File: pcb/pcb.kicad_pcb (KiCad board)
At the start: 2 copper layers, 63 parts, among them J1 AMT0440007DB0000G, J10 Conn_02x10_Odd_Even, J11 Conn_01x03, J12 Conn_01x02, J15 Conn_01x10, J16 Conn_01x10, J2 AMT0440007DB0000G, J3 AMT0440007DB0000G, J4 AMT0440007DB0000G, J5 Conn_01x03, J6 Conn_01x03, J7 Conn_01x03, J8 Conn_01x03, J9 Conn_01x03, Q1 IRF9Z34NPBF, Q2 IRF9Z34NPBF, Q3 IRF9Z34NPBF, Q4 IRF9Z34NPBF, Q5 IRF9Z34NPBF, U1 ACS711ELCTR-12AB-T, U2 ACS711ELCTR-12AB-T, U3 ACS711ELCTR-12AB-T, U4 ACS711ELCTR-12AB-T, U5 ACS711ELCTR-12AB-T, U6 TXS0102DCUR, U7 TXS0102DCUR, U8 TXS0102DCUR, U9 NCP718BSNADJT1G

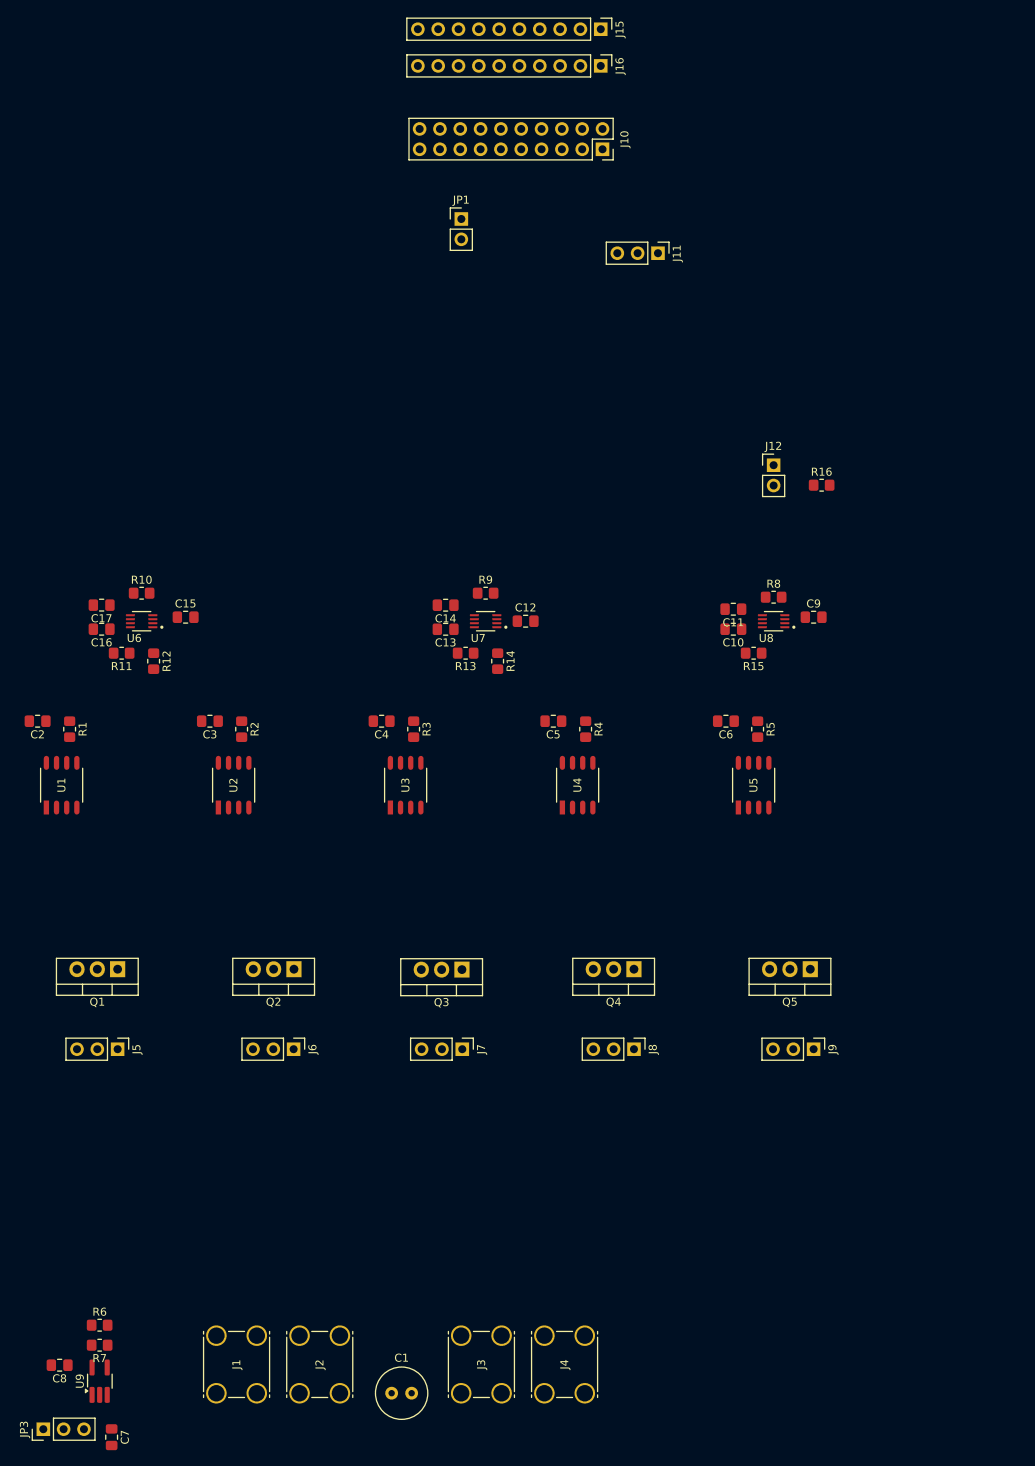
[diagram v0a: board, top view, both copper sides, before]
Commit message: Add missing power supply ctrl header and move STM32 header labels
The header for connecting the power supply control wires to the PCB was
missing from the schematic. This commit adds that header and makes the
schematic more clear with respect to the JST connector signals, the
signals associated with the wires from the JST connector, and the
signals that are routed to the STM32.

This commit also rearranges the STM32 header labels to be easier to
route.
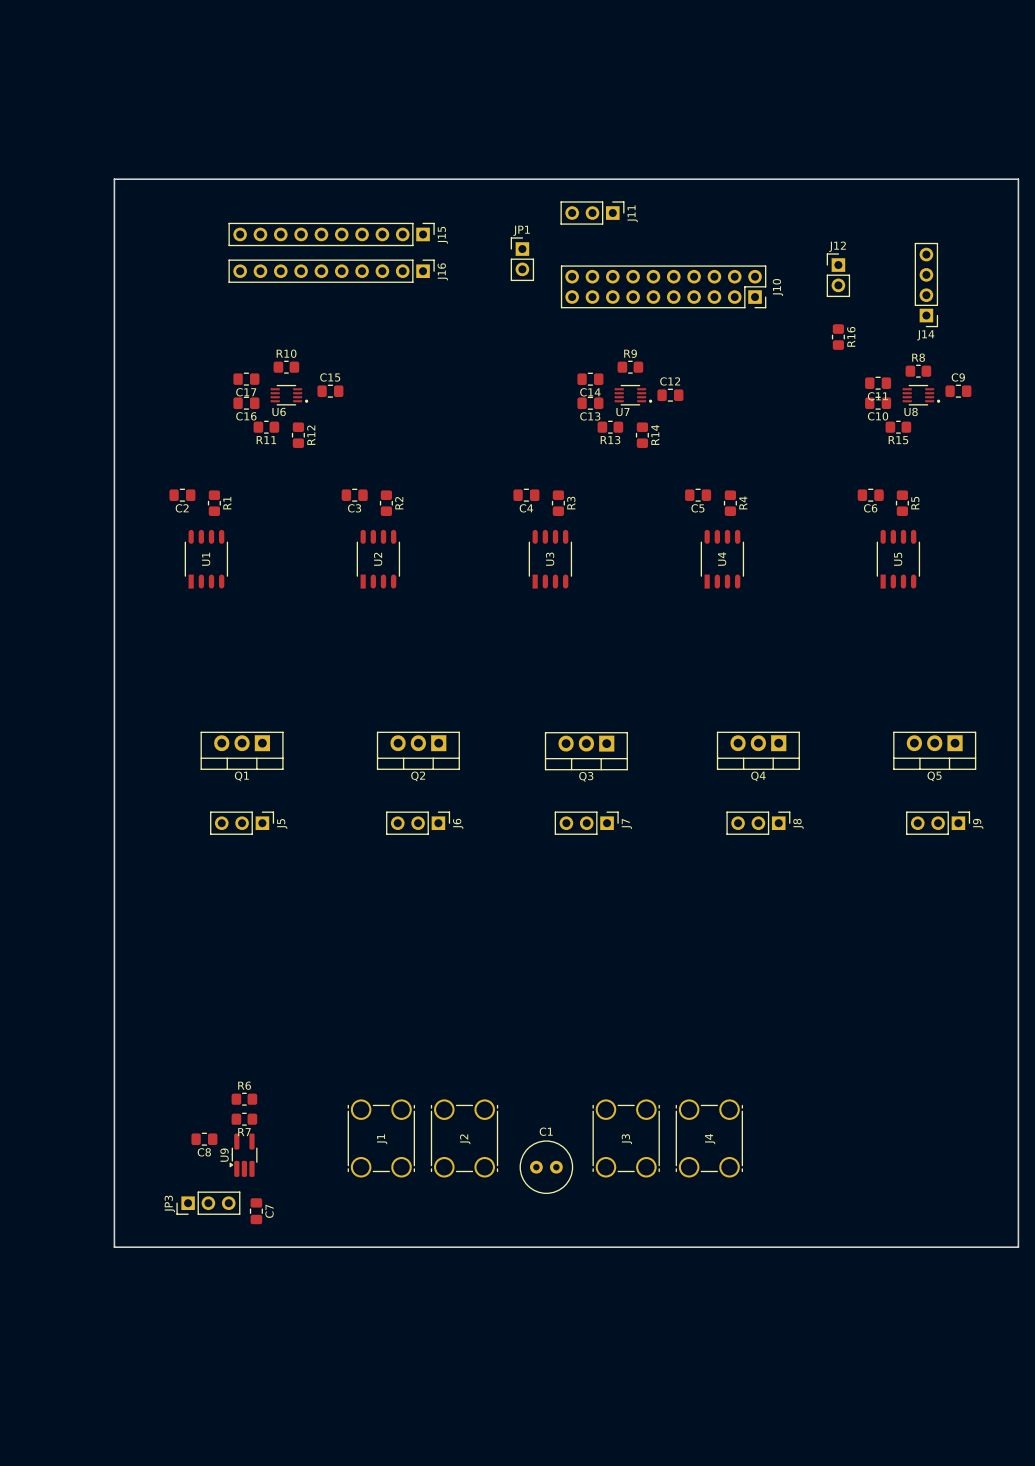
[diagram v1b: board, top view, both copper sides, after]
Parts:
- added J14: Conn_01x04, Connector_PinHeader_2.54mm:PinHeader_1x04_P2.54mm_Vertical, F.Cu at (193.1, 42.8)
- moved J16 33.9 mm to (130.2, 37.2)
- moved J15 33.9 mm to (130.2, 32.7)
- moved C13 33.5 mm to (151.1, 53.8)
- moved J2 33.5 mm to (132.8, 149.3)
- moved JP3 33.5 mm to (100.8, 153.8)
- moved C1 33.5 mm to (144.3, 149.2)
- moved C10 33.5 mm to (187.1, 53.8)
- moved C11 33.5 mm to (187.1, 51.2)
- moved C12 33.5 mm to (161.1, 52.8)
- moved C14 33.5 mm to (151.1, 50.8)
- moved C15 33.5 mm to (118.6, 52.2)
- moved C16 33.5 mm to (108.1, 53.8)
- moved C2 33.5 mm to (100.1, 65.2)
- moved C3 33.5 mm to (121.6, 65.2)
- moved C4 33.5 mm to (143.1, 65.2)
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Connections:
- J10 pad 1: CTRL_HIP -> I_SENSE_ELBOW
- J10 pad 10: I_SENSE_HAND -> SHUTOFF_WRIST_L
- J10 pad 11: SHUTOFF_HIP_L -> CTRL_HAND
- J10 pad 12: Net-(J10-Pin_12) -> I_SENSE_WRIST
- J10 pad 13: SHUTOFF_SHOULDER_L -> I_SENSE_HIP
- J10 pad 14: UART_STM_RX -> Net-(J10-Pin_14)
- J10 pad 15: SHUTOFF_ELBOW_L -> SHUTOFF_HIP_L
- J10 pad 16: UART_STM_TX -> UART_STM_RX
- J10 pad 17: SHUTOFF_WRIST_L -> CTRL_HIP
- J10 pad 18: +3V3 -> UART_STM_TX
- J10 pad 19: SHUTOFF_HAND_L -> +3V3
- J10 pad 2: I_SENSE_HIP -> CTRL_SHOULDER
- J10 pad 3: CTRL_HAND -> SHUTOFF_ELBOW_L
- J10 pad 4: I_SENSE_SHOULDER -> SHUTOFF_SHOULDER_L
- J10 pad 6: I_SENSE_ELBOW -> I_SENSE_SHOULDER
- J10 pad 7: CTRL_WRIST -> I_SENSE_HAND
- J10 pad 8: I_SENSE_WRIST -> CTRL_WRIST
- J10 pad 9: CTRL_SHOULDER -> SHUTOFF_HAND_L
- JP1 pad 1: Net-(J10-Pin_12) -> Net-(J10-Pin_14)
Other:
- board outline added: 113 x 133.5 mm

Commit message: Move +5V regulator to low power side of PCB
The +5V regulator was a bit cramped on the high-power side of the board
with the +7V and ground planes. Moving it to the low side gives those
planes more room and brings the +5V source closer to where it's used.
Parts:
- moved C7 102.1 mm to (96.5, 53.5), turned to 180 degrees
- moved C8 96.2 mm to (96.5, 49.8)
- moved R6 96.2 mm to (101.5, 44.8)
- moved R7 96.2 mm to (101.5, 47.3)
- moved U9 96.2 mm to (101.5, 51.8)
- moved JP3 95.3 mm to (102.5, 58.5), turned to -90 degrees
- moved R16 14.4 mm to (196.5, 45.5)
- moved C1 7.75 mm to (144.3, 141.5)
- moved J1 7.75 mm to (122.4, 141.5)
- moved J2 7.75 mm to (132.8, 141.5)
- moved J3 7.75 mm to (153.0, 141.5)
- moved J4 7.75 mm to (163.4, 141.5)
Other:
- board size 113 x 133.5 mm -> 110 x 123.8 mm

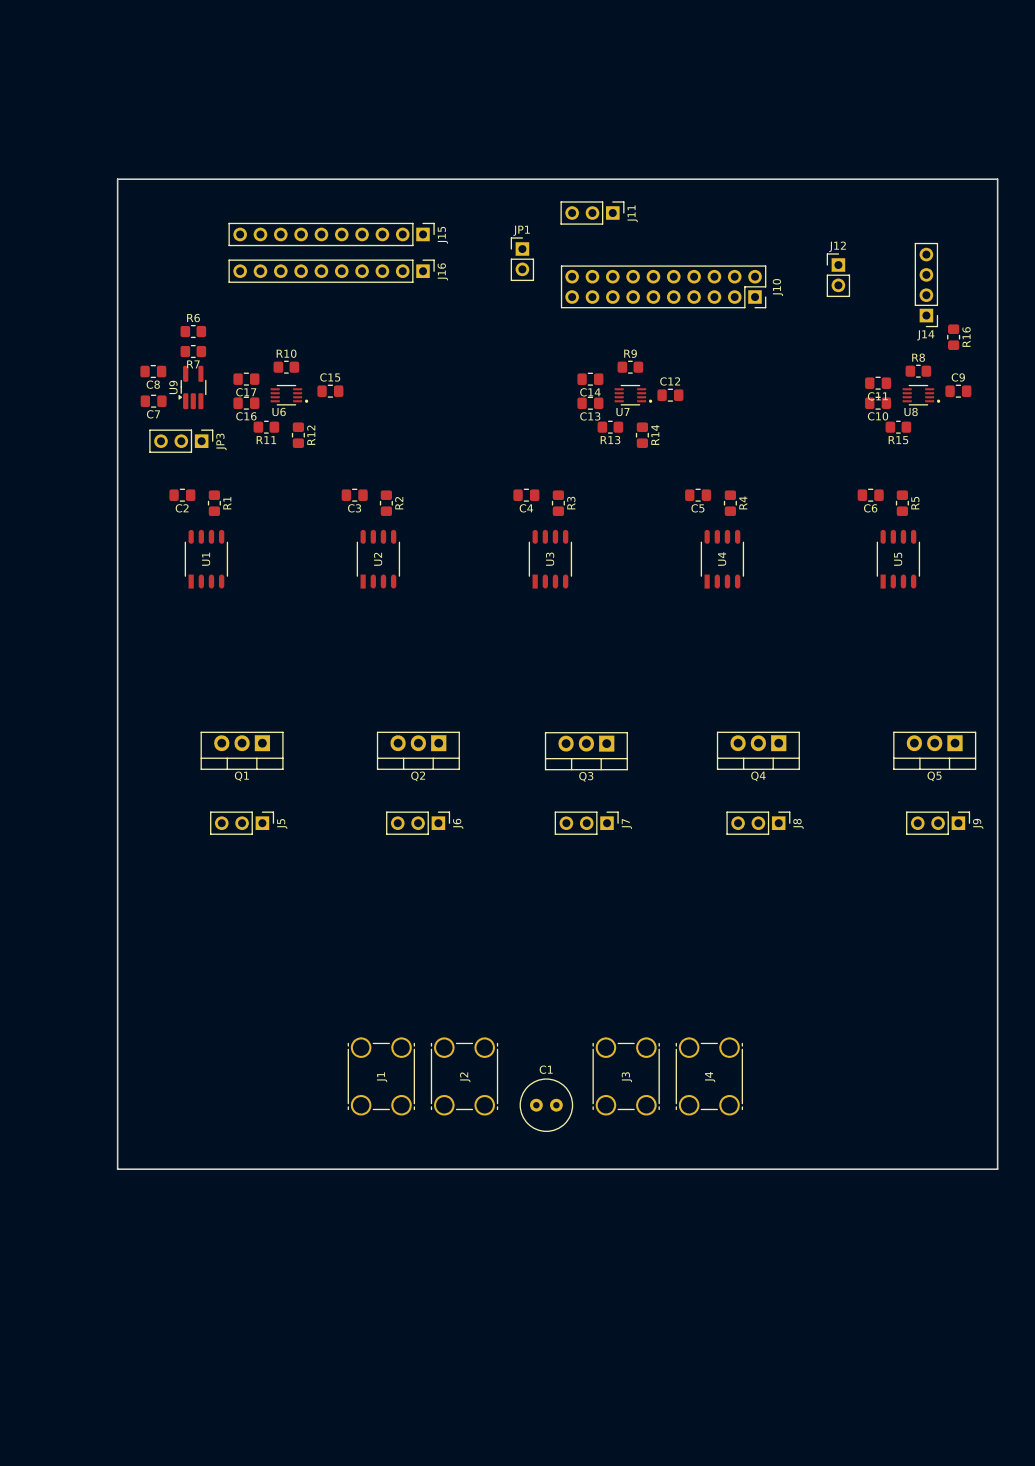
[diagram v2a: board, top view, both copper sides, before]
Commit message: Add layout for +7V components
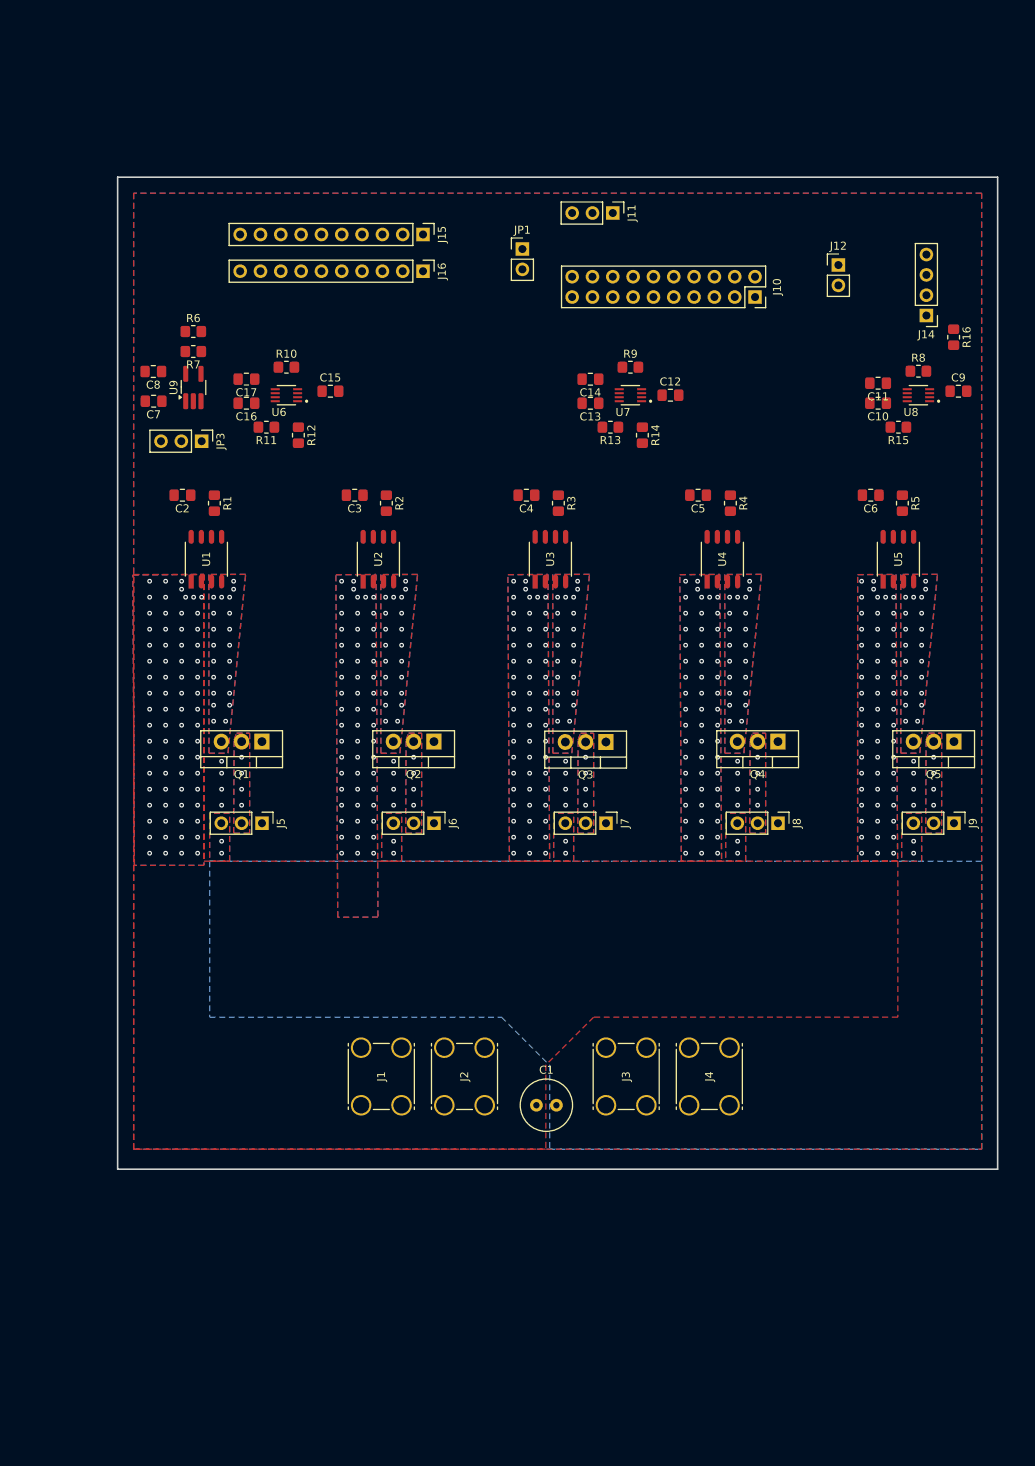
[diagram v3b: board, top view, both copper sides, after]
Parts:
- moved Q2 0.63 mm to (131.5, 96.0)
- moved J6 0.56 mm to (131.5, 106.2)
- moved J9 0.56 mm to (196.5, 106.2)
- moved Q5 0.24 mm to (196.5, 96.0)
- moved Q3 0.22 mm to (153.0, 96.1)
- moved Q4 0.22 mm to (174.5, 96.0)
- moved Q1 0.21 mm to (110.0, 96.0)
- moved J7 0.14 mm to (153.0, 106.2)
- moved J8 0.09 mm to (174.5, 106.2)
- moved J5 0.05 mm to (110.0, 106.2)
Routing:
- net Net-(J9-Pin_2): vias 0 -> 4
- net Net-(J8-Pin_2): vias 0 -> 4
- net Net-(J7-Pin_2): vias 0 -> 4
- net Net-(J6-Pin_2): vias 0 -> 4
- net Net-(J5-Pin_2): vias 0 -> 4
- net GNDREF: vias 0 -> 30
- net +7V_WRIST: vias 0 -> 21
- net +7V_SHOULDER: vias 0 -> 21
- net +7V_HIP: vias 0 -> 21
- net +7V_HAND: vias 0 -> 21
- net +7V_ELBOW: vias 0 -> 21
- net +7V: vias 0 -> 293
- added copper zone on B.Cu, net +7V
- added copper zone on F.Cu, net +7V
- added copper zone on B.Cu, net +7V_ELBOW
- added copper zone on F.Cu, net +7V_ELBOW
- added copper zone on B.Cu, net +7V_HAND
- added copper zone on F.Cu, net +7V_HAND
- added copper zone on B.Cu, net +7V_HIP
- added copper zone on F.Cu, net +7V_HIP
- added copper zone on B.Cu, net +7V_SHOULDER
- added copper zone on F.Cu, net +7V_SHOULDER
- added copper zone on B.Cu, net +7V_WRIST
- added copper zone on F.Cu, net +7V_WRIST
- added copper zone on B.Cu, net GNDREF
- added copper zone on F.Cu, net GNDREF
- added copper zone on B.Cu, net Net-(J5-Pin_2)
- added copper zone on F.Cu, net Net-(J5-Pin_2)
- added copper zone on B.Cu, net Net-(J6-Pin_2)
- added copper zone on F.Cu, net Net-(J6-Pin_2)
- added copper zone on B.Cu, net Net-(J7-Pin_2)
- added copper zone on F.Cu, net Net-(J7-Pin_2)
- added copper zone on B.Cu, net Net-(J8-Pin_2)
- added copper zone on F.Cu, net Net-(J8-Pin_2)
- added copper zone on B.Cu, net Net-(J9-Pin_2)
- added copper zone on F.Cu, net Net-(J9-Pin_2)
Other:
- board size 110 x 123.8 mm -> 110 x 124 mm

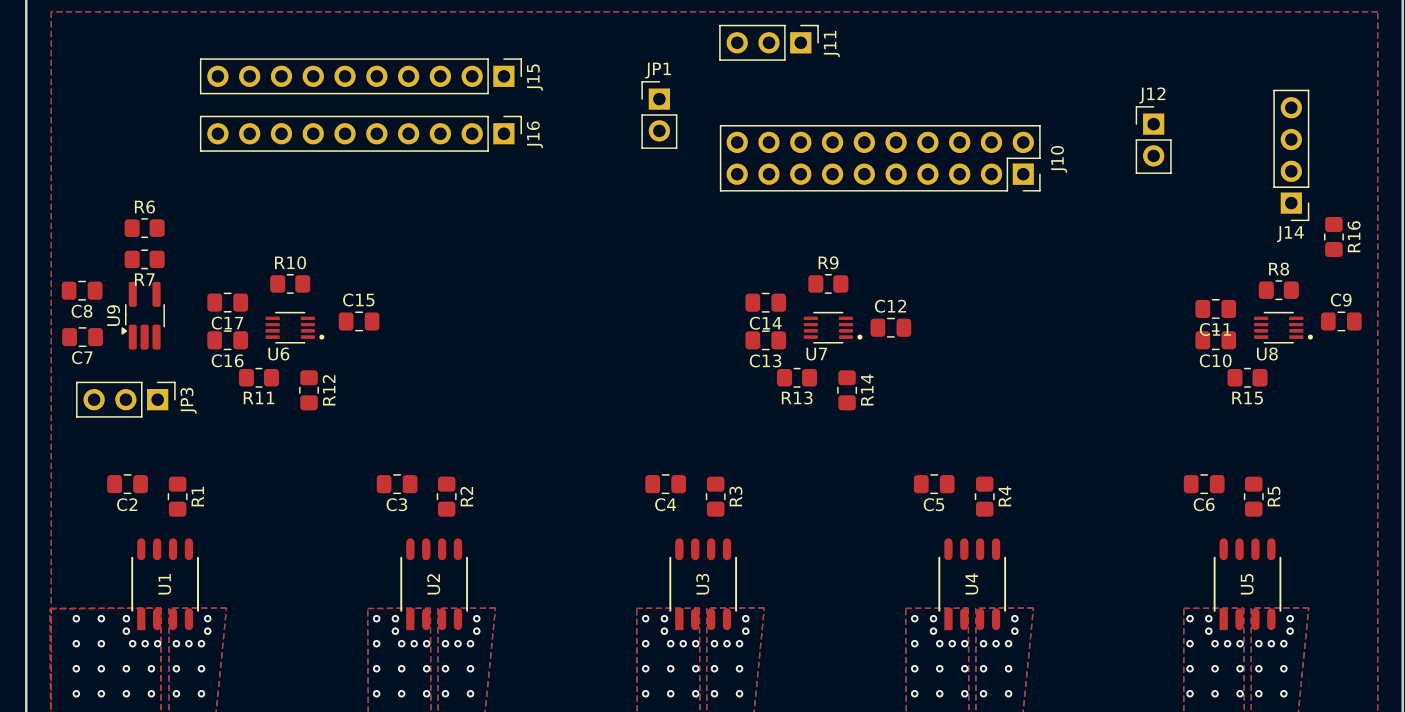
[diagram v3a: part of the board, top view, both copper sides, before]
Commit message: Add some easy traces
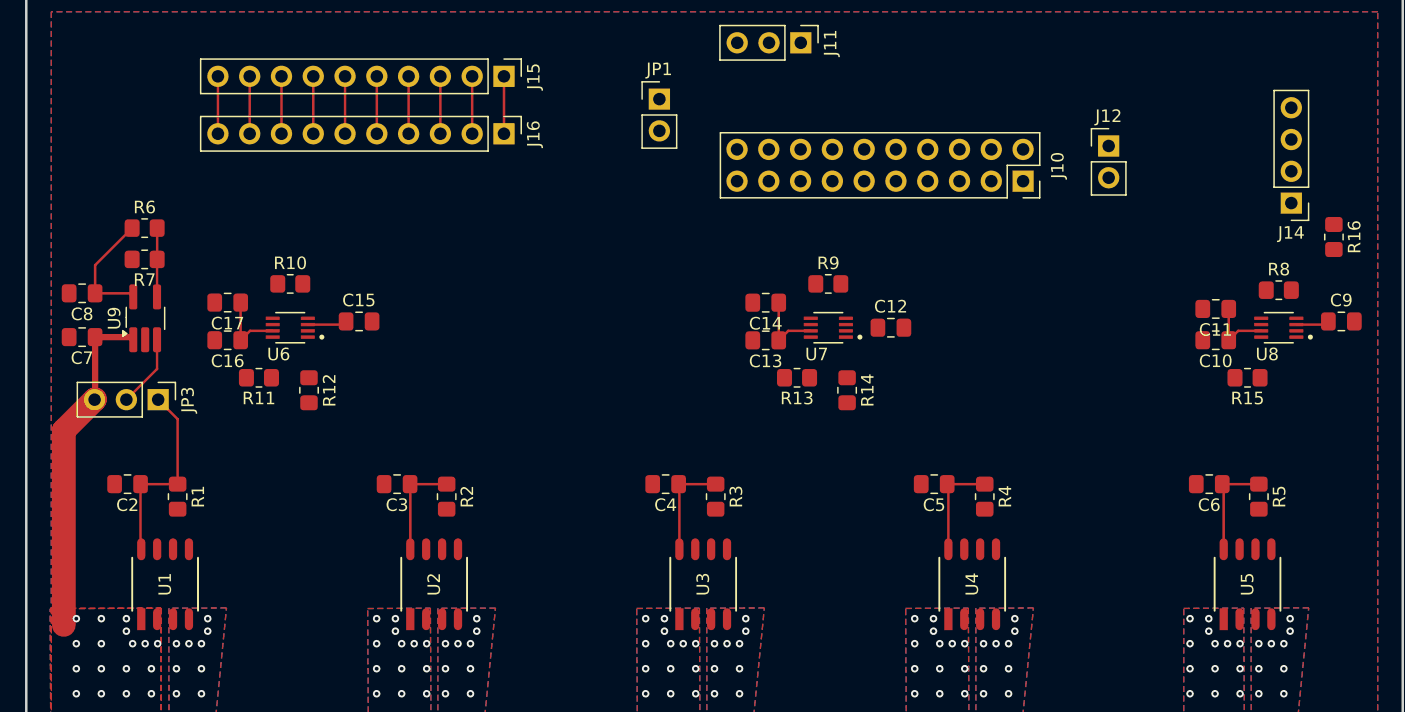
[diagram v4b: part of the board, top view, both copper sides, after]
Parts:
- moved J12 4.00 mm to (178.5, 38.2)
- moved J10 0.56 mm to (171.7, 41.0)
- moved C6 0.41 mm to (186.5, 65.2)
- moved R5 0.41 mm to (190.5, 66.2)
- moved U9 0.21 mm to (101.5, 52.0)
- moved C8 0.21 mm to (96.5, 50.0)
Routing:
- net +3V3: track 0.00 -> 54.2 mm
- net +7V: track 0.00 -> 27.2 mm
- net +5V: track 0.00 -> 26.8 mm
- net Net-(JP3-C): track 0.00 -> 5.80 mm
- net Net-(U9-ADJ): track 0.00 -> 5.50 mm
- net Net-(J15-Pin_9): track 0.00 -> 4.59 mm
- net Net-(J15-Pin_8): track 0.00 -> 4.59 mm
- net Net-(J15-Pin_7): track 0.00 -> 4.59 mm
- net Net-(J15-Pin_6): track 0.00 -> 4.59 mm
- net Net-(J15-Pin_5): track 0.00 -> 4.59 mm
- net Net-(J15-Pin_4): track 0.00 -> 4.59 mm
- net Net-(J15-Pin_3): track 0.00 -> 4.59 mm
- net Net-(J15-Pin_2): track 0.00 -> 4.59 mm
- net Net-(J15-Pin_10): track 0.00 -> 4.59 mm
- net Net-(J15-Pin_1): track 0.00 -> 4.59 mm
